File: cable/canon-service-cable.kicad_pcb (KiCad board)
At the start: 2 copper layers, 12 x 33.4 mm, 3 parts, among them J1 Conn_02x04_Odd_Even, U1 service_connector

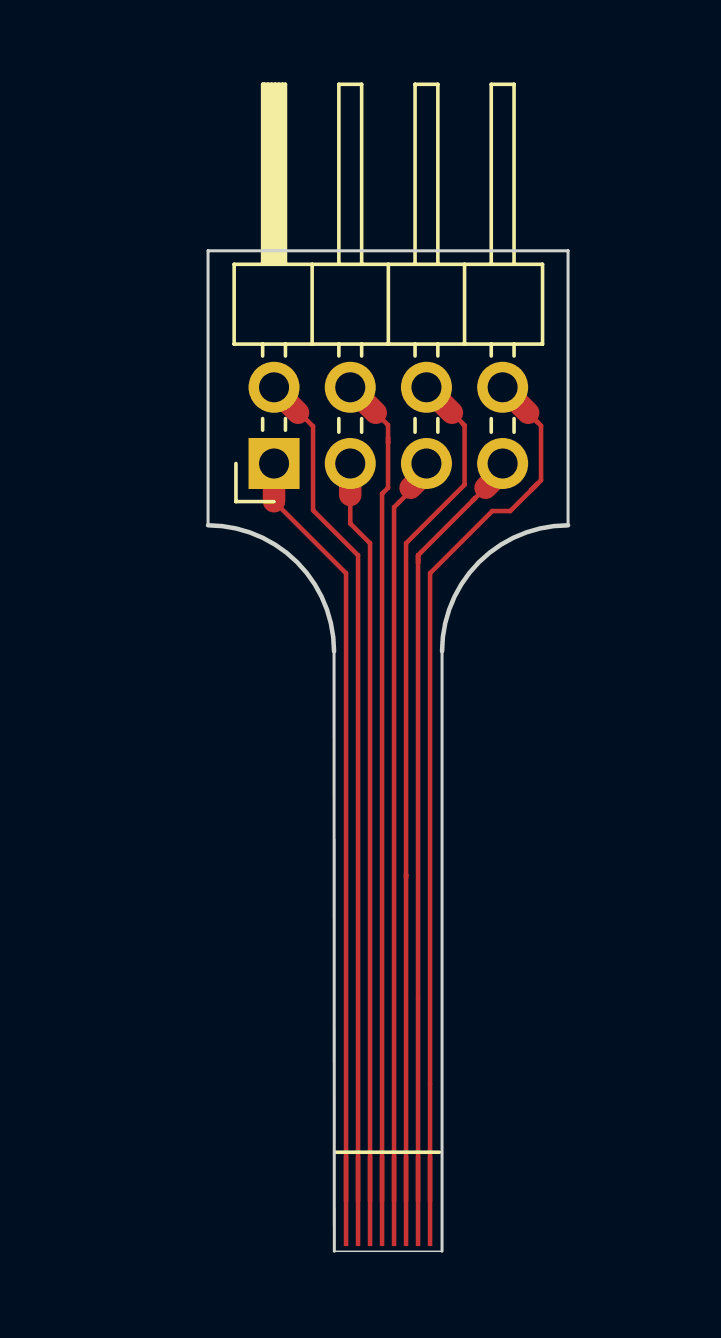
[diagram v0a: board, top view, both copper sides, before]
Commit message: cable: adjust connector width from 2.6mm to 2.7mm
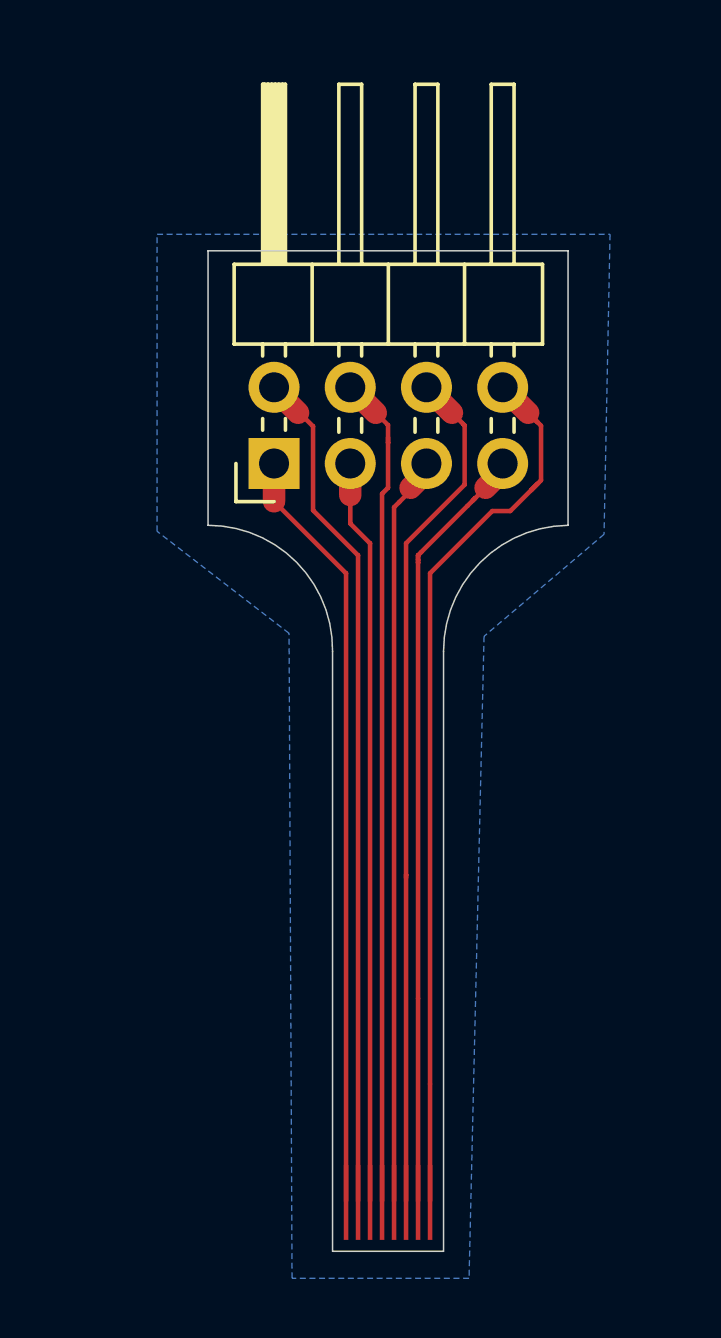
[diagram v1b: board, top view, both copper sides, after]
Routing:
- added copper zone on B.Cu, net (none)
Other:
- outline, holes or cut-outs redrawn
- board text added: "10/2020"
- board text added: "Rev. 2"
- board text removed: "09/2020"
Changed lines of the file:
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@@
     (visible_elements FFFFFF7F)
     (pcbplotparams
-      (layerselection 0x01020_ffffffff)
+      (layerselection 0x010f0_ffffffff)
       (usegerberextensions true)
       (usegerberattributes true)
@@
       (padsonsilk false)
       (subtractmaskfromsilk false)
-      (outputformat 4)
+      (outputformat 1)
       (mirror false)
       (drillshape 0)
@@
     (add_net /8)
   )
+  (module canon-service-cable:service_connector_pads (layer F.Cu)
+    (at 48.25 74.57)
+    (fp_text reference U1 (at 0 -3.85) (layer F.SilkS) hide
+      (effects (font (size 1 1) (thickness 0.15)))
+    )
+    (fp_text value service_connector (at 2.25 -2.55) (layer F.Fab)
+      (effects (font (size 1 1) (thickness 0.15)))
+    )
+    (pad 8 smd rect (at 3.15 0) (size 0.1524 2.5) (layers F.Cu F.Paste F.Mask)
+      (net 8 /8))
+    (pad 7 smd rect (at 2.75 0) (size 0.1524 2.5) (layers F.Cu F.Paste F.Mask)
+      (net 7 /7))
+    (pad 6 smd rect (at 2.35 0) (size 0.1524 2.5) (layers F.Cu F.Paste F.Mask)
+      (net 6 /6))
+    (pad 5 smd rect (at 1.95 0) (size 0.1524 2.5) (layers F.Cu F.Paste F.Mask)
+      (net 5 /5))
+    (pad 4 smd rect (at 1.55 0) (size 0.1524 2.5) (layers F.Cu F.Paste F.Mask)
+      (net 4 /4))
+    (pad 3 smd rect (at 1.15 0) (size 0.1524 2.5) (layers F.Cu F.Paste F.Mask)
+      (net 3 /3))
+    (pad 2 smd rect (at 0.75 0) (size 0.1524 2.5) (layers F.Cu F.Paste F.Mask)
+      (net 2 /2))
+    (pad 1 smd rect (at 0.35 0) (size 0.1524 2.5) (layers F.Cu F.Paste F.Mask)
+      (net 1 /1))
+  )
   (module canon-service-cable:logo (layer B.Cu)
-    (at 48.1076 54 180)
+    (at 48.11 54 180)
     (fp_text reference G1 (at 0 0) (layer B.SilkS) hide
       (effects (font (size 1.524 1.524) (thickness 0.3)) (justify mirror))
@@
       (effects (font (size 1.524 1.524) (thickness 0.3)) (justify mirror))
     )
-    (fp_poly (pts (xy -1.871133 0.6096) (xy -1.659467 0.6096) (xy -1.534165 0.606825) (xy -1.471682 0.589765)
-      (xy -1.450177 0.545316) (xy -1.4478 0.4826) (xy -1.4478 0.3556) (xy -2.167467 0.3556)
-      (xy -2.167467 1.6256) (xy -1.871133 1.6256) (xy -1.871133 0.6096)) (layer B.SilkS) (width 0.01))
-    (fp_poly (pts (xy -2.909821 1.350043) (xy -2.886659 1.208764) (xy -2.85749 1.123154) (xy -2.8292 1.100156)
-      (xy -2.808674 1.146712) (xy -2.802467 1.241807) (xy -2.793624 1.374776) (xy -2.776008 1.493308)
-      (xy -2.754386 1.57258) (xy -2.714453 1.611532) (xy -2.631104 1.62443) (xy -2.543175 1.6256)
-      (xy -2.3368 1.6256) (xy -2.3368 0.3556) (xy -2.5908 0.3556) (xy -2.5908 0.757766)
-      (xy -2.595023 0.947463) (xy -2.606777 1.083716) (xy -2.624696 1.153525) (xy -2.633133 1.159933)
-      (xy -2.667764 1.124554) (xy -2.675467 1.076996) (xy -2.681518 0.995918) (xy -2.697475 0.859116)
-      (xy -2.720044 0.694497) (xy -2.722946 0.674829) (xy -2.751374 0.507806) (xy -2.77921 0.409498)
-      (xy -2.812477 0.364212) (xy -2.845417 0.3556) (xy -2.895843 0.364125) (xy -2.93094 0.399907)
-      (xy -2.956314 0.478256) (xy -2.977575 0.614484) (xy -2.993895 0.760973) (xy -3.019233 0.961471)
-      (xy -3.043769 1.078453) (xy -3.065678 1.11179) (xy -3.083138 1.061351) (xy -3.094326 0.927008)
-      (xy -3.097513 0.76835) (xy -3.0988 0.3556) (xy -3.3528 0.3556) (xy -3.3528 1.6256)
-      (xy -2.93933 1.6256) (xy -2.909821 1.350043)) (layer B.SilkS) (width 0.01))
     (fp_poly (pts (xy -1.741838 2.754445) (xy -1.625447 2.721626) (xy -1.537565 2.660606) (xy -1.459613 2.56479)
       (xy -1.423442 2.509544) (xy -1.344963 2.404804) (xy -1.250776 2.32673) (xy -1.124916 2.268621)
@@
       (xy -2.330905 2.753629) (xy -2.136225 2.761787) (xy -2.134465 2.761847) (xy -1.905318 2.765654)
       (xy -1.741838 2.754445)) (layer B.SilkS) (width 0.01))
-  )
-  (module canon-service-cable:service_connector_pads (layer F.Cu)
-    (at 48.25 74.5236)
-    (fp_text reference U1 (at 0 -3.85) (layer F.SilkS) hide
-      (effects (font (size 1 1) (thickness 0.15)))
-    )
-    (fp_text value service_connector (at 2.25 -2.55) (layer F.Fab)
-      (effects (font (size 1 1) (thickness 0.15)))
-    )
-    (pad 8 smd rect (at 3.15 0) (size 0.1524 3) (layers F.Cu F.Paste F.Mask)
-      (net 8 /8))
-    (pad 7 smd rect (at 2.75 0) (size 0.1524 3) (layers F.Cu F.Paste F.Mask)
-      (net 7 /7))
-    (pad 6 smd rect (at 2.35 0) (size 0.1524 3) (layers F.Cu F.Paste F.Mask)
-      (net 6 /6))
-    (pad 5 smd rect (at 1.95 0) (size 0.1524 3) (layers F.Cu F.Paste F.Mask)
-      (net 5 /5))
-    (pad 4 smd rect (at 1.55 0) (size 0.1524 3) (layers F.Cu F.Paste F.Mask)
-      (net 4 /4))
-    (pad 3 smd rect (at 1.15 0) (size 0.1524 3) (layers F.Cu F.Paste F.Mask)
-      (net 3 /3))
-    (pad 2 smd rect (at 0.75 0) (size 0.1524 3) (layers F.Cu F.Paste F.Mask)
-      (net 2 /2))
-    (pad 1 smd rect (at 0.35 0) (size 0.1524 3) (layers F.Cu F.Paste F.Mask)
-      (net 1 /1))
+    (fp_poly (pts (xy -2.909821 1.350043) (xy -2.886659 1.208764) (xy -2.85749 1.123154) (xy -2.8292 1.100156)
+      (xy -2.808674 1.146712) (xy -2.802467 1.241807) (xy -2.793624 1.374776) (xy -2.776008 1.493308)
+      (xy -2.754386 1.57258) (xy -2.714453 1.611532) (xy -2.631104 1.62443) (xy -2.543175 1.6256)
+      (xy -2.3368 1.6256) (xy -2.3368 0.3556) (xy -2.5908 0.3556) (xy -2.5908 0.757766)
+      (xy -2.595023 0.947463) (xy -2.606777 1.083716) (xy -2.624696 1.153525) (xy -2.633133 1.159933)
+      (xy -2.667764 1.124554) (xy -2.675467 1.076996) (xy -2.681518 0.995918) (xy -2.697475 0.859116)
+      (xy -2.720044 0.694497) (xy -2.722946 0.674829) (xy -2.751374 0.507806) (xy -2.77921 0.409498)
+      (xy -2.812477 0.364212) (xy -2.845417 0.3556) (xy -2.895843 0.364125) (xy -2.93094 0.399907)
+      (xy -2.956314 0.478256) (xy -2.977575 0.614484) (xy -2.993895 0.760973) (xy -3.019233 0.961471)
+      (xy -3.043769 1.078453) (xy -3.065678 1.11179) (xy -3.083138 1.061351) (xy -3.094326 0.927008)
+      (xy -3.097513 0.76835) (xy -3.0988 0.3556) (xy -3.3528 0.3556) (xy -3.3528 1.6256)
+      (xy -2.93933 1.6256) (xy -2.909821 1.350043)) (layer B.SilkS) (width 0.01))
+    (fp_poly (pts (xy -1.871133 0.6096) (xy -1.659467 0.6096) (xy -1.534165 0.606825) (xy -1.471682 0.589765)
+      (xy -1.450177 0.545316) (xy -1.4478 0.4826) (xy -1.4478 0.3556) (xy -2.167467 0.3556)
+      (xy -2.167467 1.6256) (xy -1.871133 1.6256) (xy -1.871133 0.6096)) (layer B.SilkS) (width 0.01))
   )
   (module Connector_PinHeader_2.54mm:PinHeader_2x04_P2.54mm_Horizontal (layer F.Cu)
@@
     )
   )
+  (gr_text "Rev. 2" (at 50.1 54.9) (layer B.SilkS)
+    (effects (font (size 0.5 0.5) (thickness 0.125)) (justify mirror))
+  )
   (gr_text coon (at 50.0888 43.8404) (layer B.SilkS)
     (effects (font (size 0.75 0.75) (thickness 0.125)) (justify mirror))
   )
-  (gr_text 09/2020 (at 49.9364 45.2628) (layer B.SilkS)
+  (gr_text 10/2020 (at 49.9364 45.2628) (layer B.SilkS)
     (effects (font (size 0.75 0.75) (thickness 0.125)) (justify mirror))
   )
-  (gr_line (start 48.26 72.898) (end 51.7144 72.898) (layer F.SilkS) (width 0.12))
-  (gr_line (start 48.2092 76.2) (end 51.8 76.2) (layer Edge.Cuts) (width 0.05))
-  (gr_arc (start 56 56.2) (end 56 52) (angle -90) (layer Edge.Cuts) (width 0.15))
-  (gr_line (start 48.2092 76.2) (end 48.2 56.2) (layer Edge.Cuts) (width 0.1))
-  (gr_arc (start 44 56.2) (end 48.2 56.2) (angle -90) (layer Edge.Cuts) (width 0.15))
-  (gr_line (start 51.8 56.2) (end 51.8 76.2) (layer Edge.Cuts) (width 0.1))
-  (gr_line (start 56 42.85) (end 56 52) (layer Edge.Cuts) (width 0.1))
-  (gr_line (start 44 42.85) (end 56 42.85) (layer Edge.Cuts) (width 0.1))
-  (gr_line (start 44 52) (end 44 42.85) (layer Edge.Cuts) (width 0.1))
+  (gr_line (start 48.15 76.2) (end 51.85 76.2) (layer Edge.Cuts) (width 0.05))
+  (gr_arc (start 56.05 56.2) (end 56 52) (angle -89.31793961) (layer Edge.Cuts) (width 0.05))
+  (gr_line (start 48.15 76.2) (end 48.15 56.2) (layer Edge.Cuts) (width 0.05))
+  (gr_arc (start 44 56.15) (end 48.15 56.2) (angle -90.6902772) (layer Edge.Cuts) (width 0.05))
+  (gr_line (start 51.85 56.2) (end 51.85 76.2) (layer Edge.Cuts) (width 0.05))
+  (gr_line (start 56 42.85) (end 56 52) (layer Edge.Cuts) (width 0.05))
+  (gr_line (start 44 42.85) (end 56 42.85) (layer Edge.Cuts) (width 0.05))
+  (gr_line (start 44 52) (end 44 42.85) (layer Edge.Cuts) (width 0.05))
   (segment (start 46.2 49.94) (end 46.2 51.2) (width 0.75) (layer F.Cu) (net 1) (status 10))
   (segment (start 48.6 53.6) (end 46.2 51.2) (width 0.1524) (layer F.Cu) (net 1))
@@
   (segment (start 51.4 70.6216) (end 51.4 74.5236) (width 0.1524) (layer F.Cu) (net 8) (status 20))
   (segment (start 51.4 53.6) (end 51.4 70.6216) (width 0.1524) (layer F.Cu) (net 8))
+  (zone (net 0) (net_name "") (layer B.Cu) (hatch edge 0.508)
+    (connect_pads (clearance 0.508))
+    (min_thickness 0.254)
+    (fill yes (arc_segments 32) (thermal_gap 0.508) (thermal_bridge_width 0.508))
+    (polygon
+      (pts
+        (xy 57.2 52.3) (xy 53.2 55.7) (xy 52.7 77.1) (xy 46.8 77.1) (xy 46.7 55.6)
+        (xy 42.3 52.2) (xy 42.3 42.3) (xy 57.4 42.3)
+      )
+    )
+  )
 )

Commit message: cable: replace angled pin header by angled IDC header
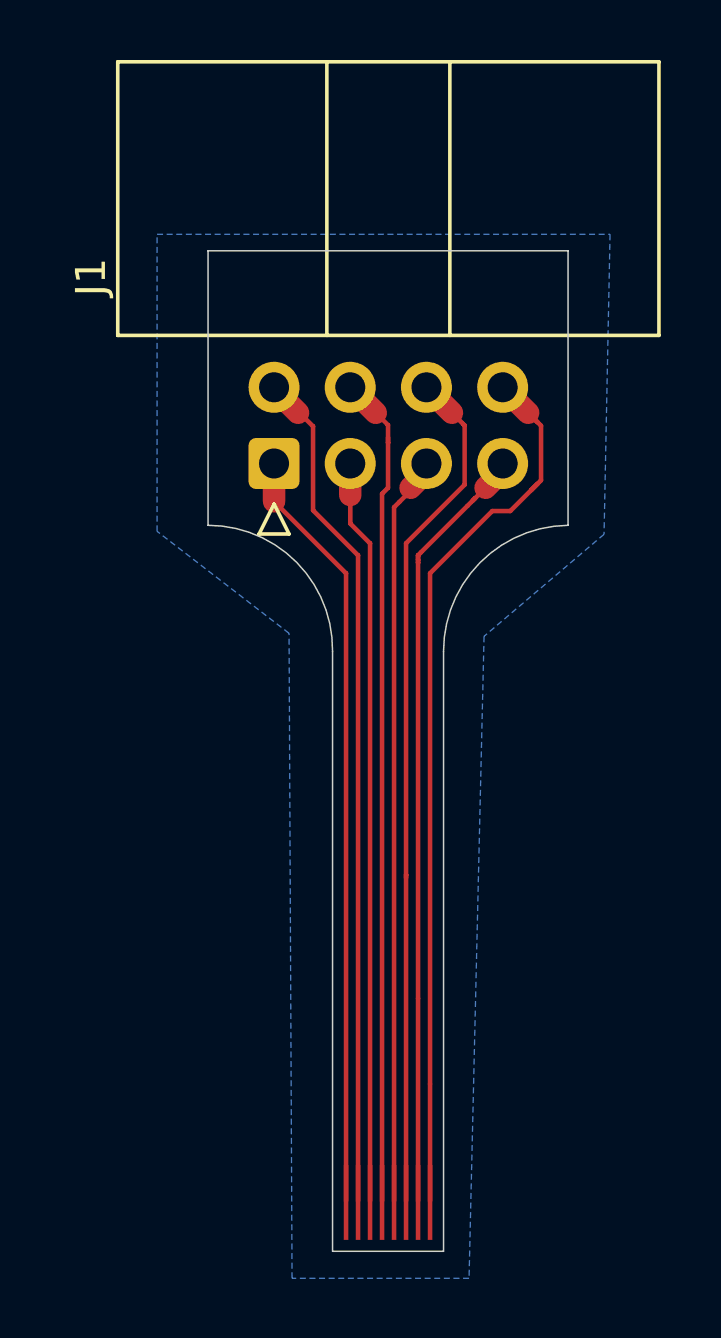
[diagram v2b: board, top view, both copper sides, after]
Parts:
- J1: footprint Connector_PinHeader_2.54mm:PinHeader_2x04_P2.54mm_Horizontal -> Connector_IDC:IDC-Header_2x04_P2.54mm_Horizontal
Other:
- board text removed: "coon"
